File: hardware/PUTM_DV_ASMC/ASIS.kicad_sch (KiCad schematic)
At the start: 0 parts

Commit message: assi section
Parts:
- added Q1, Q2: BUK6D210, Local_Library:Diodes_UDFN2020-6_Type-F, symbol BUK6D210:BUK6D210
- added R14, R16: 10k, Resistor_SMD:R_0603_1608Metric, symbol Device:R_Small
- added R15, R9: 100R, Resistor_SMD:R_0603_1608Metric, symbol Device:R_Small
- added TP1, TP2: TestPoint_Small, TestPoint:TestPoint_Pad_D1.0mm, symbol Connector:TestPoint_Small
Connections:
- new net: Q2.3 (G), R15.1, R16.2, TP2.1
- new net: Q1.3 (G), R14.2, R9.1, TP1.1
- new net DI_PIN: Q2.1 (D), Q2.2 (D), Q2.5 (D), Q2.6 (D), Q2.7 (D)
- new net DO_PIN: Q1.1 (D), Q1.2 (D), Q1.5 (D), Q1.6 (D), Q1.7 (D)
- new net GND: Q1.4 (S), Q1.8 (S), Q2.4 (S), Q2.8 (S), R14.1, R16.1
- new net IN_G: R15.2
- new net IN_R: R9.2
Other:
- note added: "WS2815"
- title: (none) -> ASSI Section

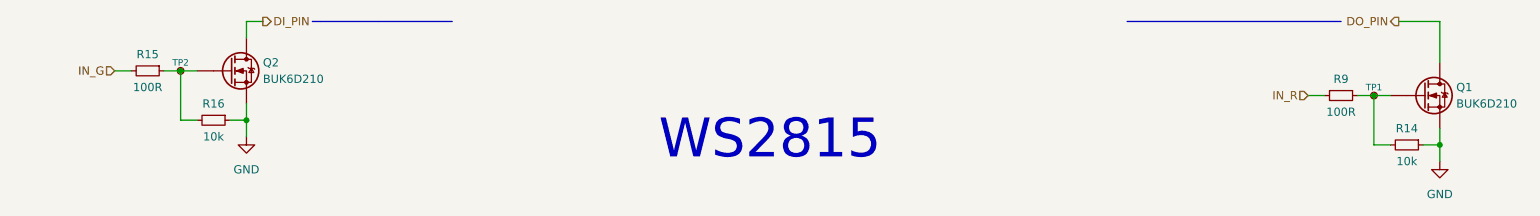
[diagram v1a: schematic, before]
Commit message: schematics without main connector
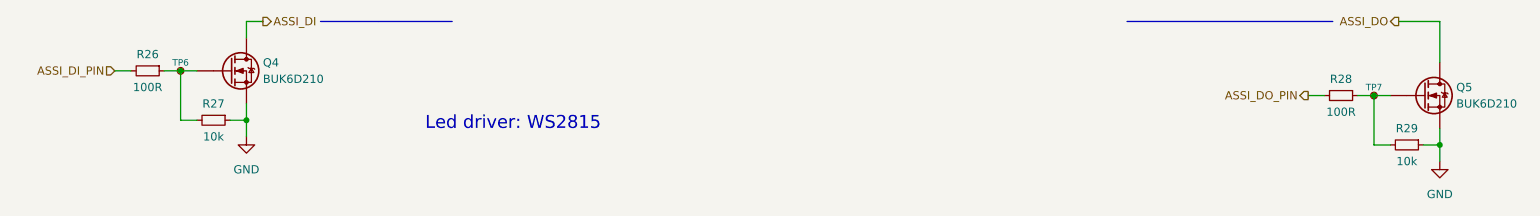
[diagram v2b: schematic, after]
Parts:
- renumbered Q2 to Q4, Q1 to Q5, R15 to R26, R16 to R27, R9 to R28, R14 to R29, TP2 to TP6, TP1 to TP7
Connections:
- net DI_PIN renamed ASSI_DI
- net DO_PIN renamed ASSI_DO
- net IN_G renamed ASSI_DI_PIN
- net IN_R renamed ASSI_DO_PIN
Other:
- note added: "Led driver: WS2815"
- note removed: "WS2815"

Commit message: done schematic v1
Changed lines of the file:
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@@
 	)
 	(hierarchical_label "ASSI_DO_PIN"
-		(shape output)
+		(shape input)
 		(at 224.79 88.9 180)
 		(effects

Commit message: schematic without error
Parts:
- Q4, Q5: footprint Local_Library:Diodes_UDFN2020-6_Type-F -> UDFN2020-6:Diodes_UDFN2020-6_Type-F
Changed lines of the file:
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@@
 			)
 		)
-		(property "Footprint" "Local_Library:Diodes_UDFN2020-6_Type-F"
+		(property "Footprint" "UDFN2020-6:Diodes_UDFN2020-6_Type-F"
 			(at 59.69 97.79 0)
 			(hide yes)
@@
 			)
 		)
-		(property "Footprint" "Local_Library:Diodes_UDFN2020-6_Type-F"
+		(property "Footprint" "UDFN2020-6:Diodes_UDFN2020-6_Type-F"
 			(at 243.84 101.6 0)
 			(hide yes)
